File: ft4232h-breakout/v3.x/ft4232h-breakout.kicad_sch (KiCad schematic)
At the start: 32 parts, among them J3 Conn_01x03, J4 Conn_01x03, J5 JLCPCB_3.5MM_SOCKET_C18166, J6 JLCPCB_3.5MM_SOCKET_C18166, J7 JLCPCB_3.5MM_SOCKET_C18166, X1 FT4232H-MODULE

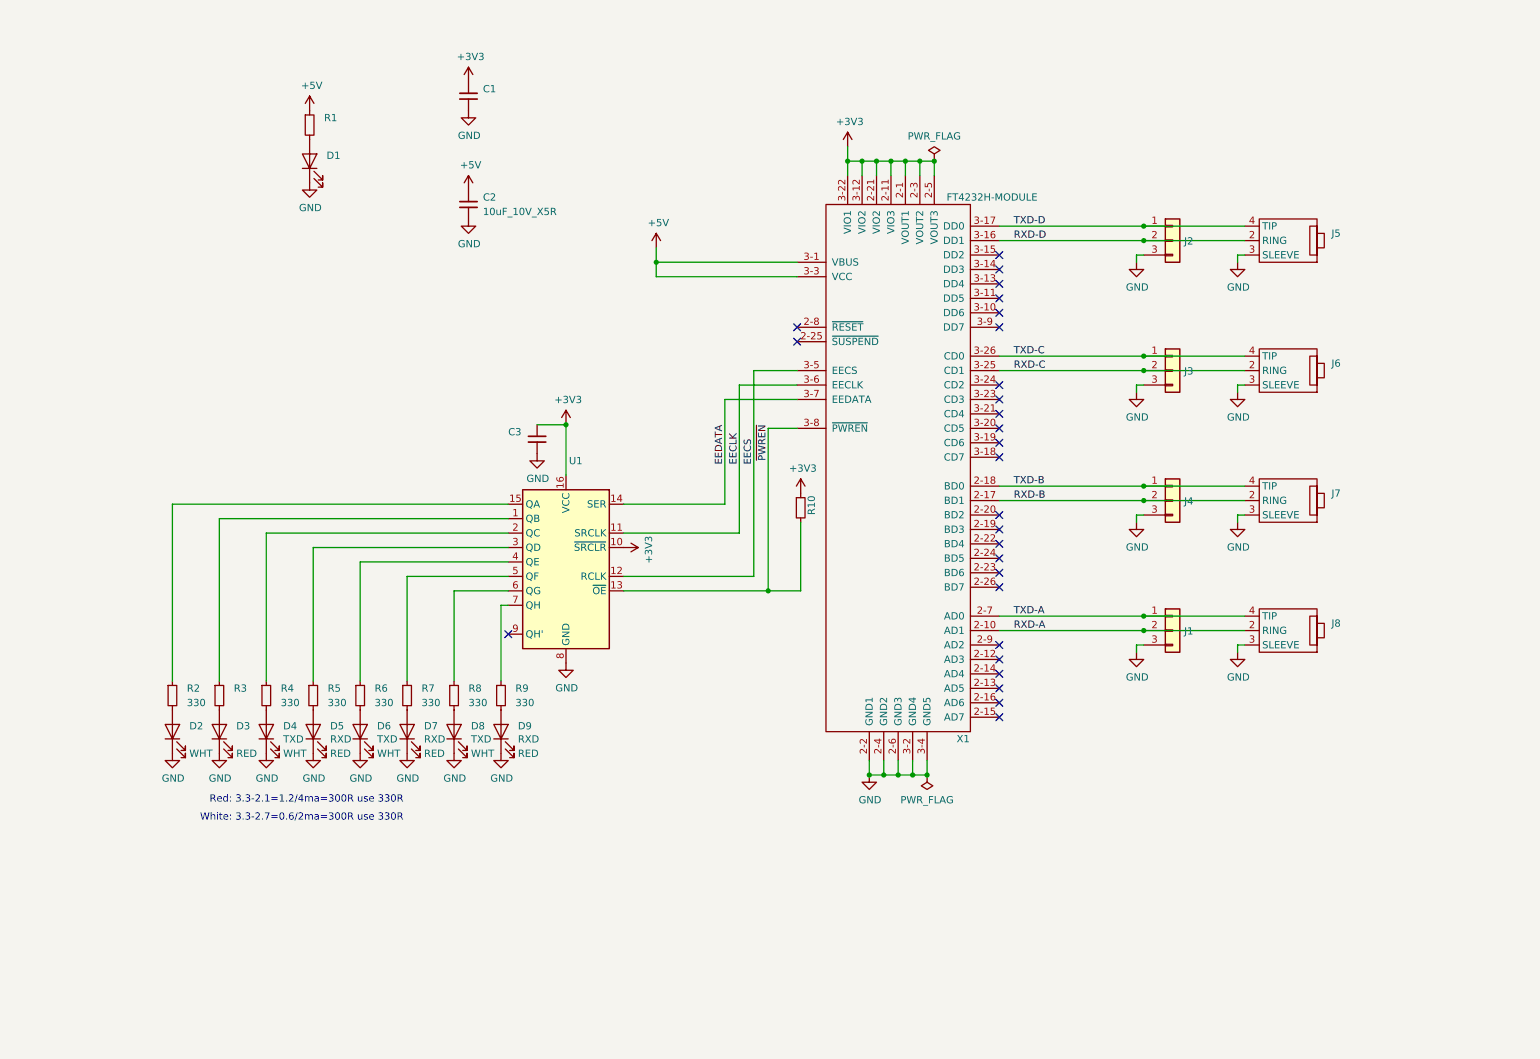
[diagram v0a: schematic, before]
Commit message: ft4232h-breakout: v3 schematic complete and reviewed
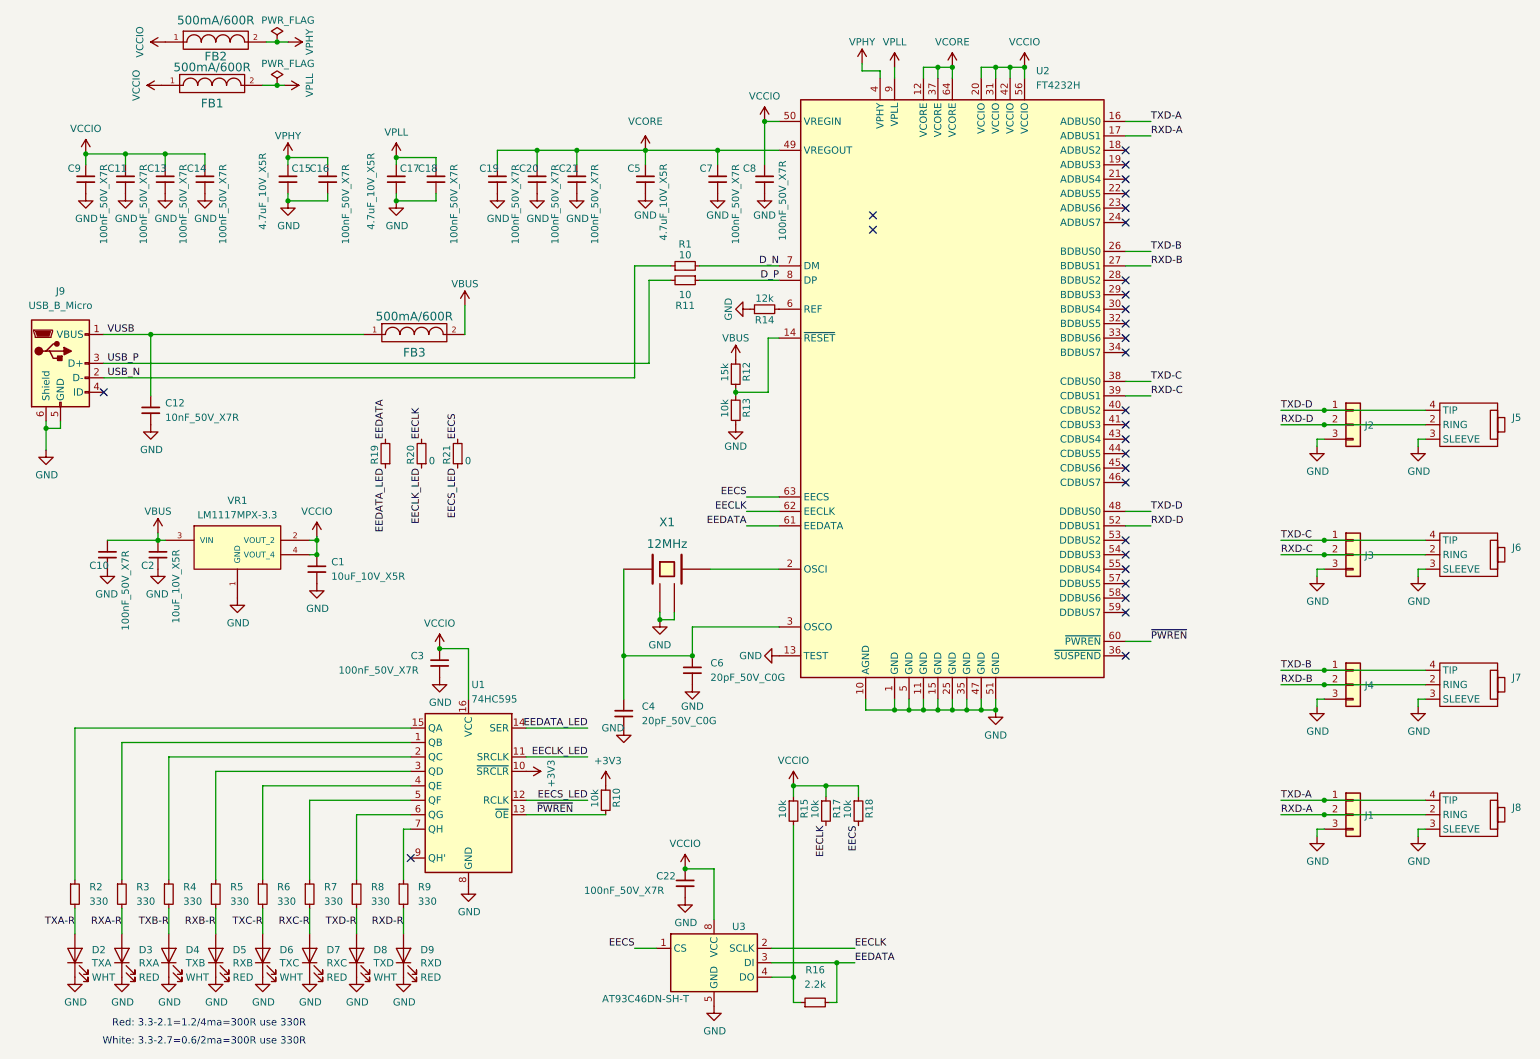
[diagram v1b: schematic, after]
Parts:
- removed D1: (no value), symbol tom-opto:LED
- removed R1: (no value), R_0402_1005Metric, symbol jlcpcb-basic-resistor-0402:1k
- removed X1: FT4232H-MODULE, tom-modules:FT4232H-MODULE, symbol tom-modules:FT4232H-MODULE
- added C10, C11, C13, C14, C16, C18, C19, C20, C21, C22, C7, C8, C9: 100nF_50V_X7R, tom-passives:C_0402_1005Metric, symbol jlcpcb-basic-capacitor-0402:100nF_50V_X7R
- added C12: 10nF_50V_X7R, tom-passives:C_0402_1005Metric, symbol jlcpcb-basic-capacitor-0402:10nF_50V_X7R
- added C15, C17, C5: 4.7uF_10V_X5R, tom-passives:C_0402_1005Metric, symbol jlcpcb-basic-capacitor-0402:4.7uF_10V_X5R
- added C4, C6: 20pF_50V_C0G, tom-passives:C_0402_1005Metric, symbol jlcpcb-basic-capacitor-0402:20pF_50V_C0G
- added FB1, FB2, FB3: 500mA/600R, tom-passives:C_0805_2012Metric, symbol tom-passives:FILTER
- added J9: USB_B_Micro, tom-connectors:USB_B_Micro_LCSC_C10418, symbol tom-connectors:USB_B_Micro
- added R1, R11: 10, tom-passives:R_0402_1005Metric, symbol jlcpcb-basic-resistor-0402:10
- added R12: 15k, tom-passives:R_0402_1005Metric, symbol jlcpcb-basic-resistor-0402:15k
- added R13, R15, R17, R18: 10k, tom-passives:R_0402_1005Metric, symbol jlcpcb-basic-resistor-0402:10k
- added R14: 12k, tom-passives:R_0402_1005Metric, symbol jlcpcb-basic-resistor-0402:12k
- added R16: 2.2k, tom-passives:R_0402_1005Metric, symbol jlcpcb-basic-resistor-0402:2.2k
- added R19: (no value), symbol jlcpcb-basic-resistor-0402:0
- added R20, R21: 0, symbol jlcpcb-basic-resistor-0402:0
- added U2: FT4232H, tom-semiconductors:TQFP-64_10x10mm_P0.5mm, symbol tom-semiconductors:FT4232H
- added U3: AT93C46DN-SH-T, tom-semiconductors:SO-8_3.9x4.9mm_P1.27mm, symbol Memory_EEPROM:93CxxA
- added VR1: LM1117MPX-3.3, tom-semiconductors:VREG_LM1117MPX-3.3, symbol tom-semiconductors:LM1117MPX-3.3
- added X1: 12MHz, tom-passives:Crystal_SMD_3225-4Pin_3.2x2.5mm, symbol tom-passives:CRYSTAL_4PIN
- C1: value (none) -> 10uF_10V_X5R; footprint C_0603_1608Metric -> tom-passives:C_0603_1608Metric
- C2: footprint C_0603_1608Metric -> tom-passives:C_0603_1608Metric
- C3: value (none) -> 100nF_50V_X7R; footprint C_0402_1005Metric -> tom-passives:C_0402_1005Metric
- D2: value (none) -> TXA; footprint (none) -> tom-opto:LED_0603_1608Metric
- D3: value (none) -> RXA; footprint (none) -> tom-opto:LED_0603_1608Metric
- D4: value TXD -> TXB
- D5: value RXD -> RXB
- D6: value TXD -> TXC
- D7: value RXD -> RXC
- J1, J2: value (none) -> Conn_01x03; footprint (none) -> tom-connectors:PinHeader_1x03_P2.54mm_Horizontal
- J8: value (none) -> JLCPCB_3.5MM_SOCKET_C18166
- R10: value (none) -> 10k; footprint R_0402_1005Metric -> tom-passives:R_0402_1005Metric
- R2, R4, R5, R6, R7, R8, R9: footprint R_0402_1005Metric -> tom-passives:R_0402_1005Metric
- R3: value (none) -> 330; footprint R_0402_1005Metric -> tom-passives:R_0402_1005Metric
- U1: value (none) -> 74HC595; footprint (none) -> tom-semiconductors:SOIC-16_4.55x10.3mm_P1.27mm
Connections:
- net +3V3: no longer C1.1, C3.2, U1.16 (VCC)
- net EECLK: now also R17.2, R20.2, U2.62 (EECLK), U3.2 (SCLK); no longer U1.11 (SRCLK)
- net EECS: now also R18.2, R21.2, U2.63 (EECS), U3.1 (CS); no longer U1.12 (RCLK)
- net EEDATA: now also R16.2, R19.2, U2.61 (EEDATA), U3.3 (DI); no longer U1.14 (SER)
- net GND: now also C10.1, C11.1, C12.2, C13.1, C14.1, C15.2, C16.1, C17.2, C18.1, C19.1, C20.1, C21.1, C22.1, C4.2, C5.2, C6.2, C7.1, C8.1, C9.1, J9.5 (GND), J9.6 (Shield), R13.2, R14.1, U2.1 (GND), U2.10 (AGND), U2.11 (GND), U2.13 (TEST), U2.15 (GND), U2.25 (GND), U2.35 (GND), U2.47 (GND), U2.5 (GND), U2.51 (GND), U3.5 (GND), VR1.1 (GND), X1.2 (GND), X1.4 (GND)
- net RXD-A: now also U2.17 (ADBUS1)
- net RXD-B: now also U2.27 (BDBUS1)
- net RXD-C: now also U2.39 (CDBUS1)
- net RXD-D: now also U2.52 (DDBUS1)
- net TXD-A: now also U2.16 (ADBUS0)
- net TXD-B: now also U2.26 (BDBUS0)
- net TXD-C: now also U2.38 (CDBUS0)
- net TXD-D: now also U2.48 (DDBUS0)
- net ~{PWREN}: now also U2.60 (~{PWREN})
- net RXD-R: now reaches D9.2 (A), R9.2
- net RXA-R: now reaches D3.2 (A), R3.2
- net TXD-R: now reaches D8.2 (A), R8.2
- net TXC-R: now reaches D6.2 (A), R6.2
- net RXB-R: now reaches D5.2 (A), R5.2
- net TXB-R: now reaches D4.2 (A), R4.2
- net TXA-R: now reaches D2.2 (A), R2.2
- net RXC-R: now reaches D7.2 (A), R7.2
- net +5V renamed VBUS
- net VBUS: now also C10.2, FB3.2, R12.1, VR1.3 (VIN)
- new net: C4.1, C6.1, U2.3 (OSCO), X1.1
- new net: U2.2 (OSCI), X1.3
- new net: R15.2, R16.1, U3.4 (DO)
- new net: R12.2, R13.1, U2.14 (~{RESET})
- new net: R14.2, U2.6 (REF)
- new net D_N: R1.2, U2.7 (DM)
- new net D_P: R11.1, U2.8 (DP)
- new net EECLK_LED: R20.1, U1.11 (SRCLK)
- new net EECS_LED: R21.1, U1.12 (RCLK)
- new net EEDATA_LED: R19.1, U1.14 (SER)
- new net USB_N: J9.2 (D-), R1.1
- new net USB_P: J9.3 (D+), R11.2
- new net VCCIO: C1.1, C11.2, C13.2, C14.2, C22.2, C3.2, C8.2, C9.2, FB1.1, FB2.1, R15.1, R17.1, R18.1, U1.16 (VCC), U2.20 (VCCIO), U2.31 (VCCIO), U2.42 (VCCIO), U2.50 (VREGIN), U2.56 (VCCIO), U3.8 (VCC), VR1.2 (VOUT_2), VR1.4 (VOUT_4)
- new net VCORE: C19.2, C20.2, C21.2, C5.1, C7.2, U2.12 (VCORE), U2.37 (VCORE), U2.49 (VREGOUT), U2.64 (VCORE)
- new net VPHY: C15.1, C16.2, FB2.2, U2.4 (VPHY)
- new net VPLL: C17.1, C18.2, FB1.2, U2.9 (VPLL)
- new net VUSB: C12.1, FB3.1, J9.1 (VBUS)
- no-connect marks 27 -> 29
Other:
- moved on the sheet: C1, C2, C3, D2, D3, D4, D5, D6, D7, D8, D9, J1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

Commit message: ft4232h-breakout: v3 at rc1
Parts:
- added D1: LED, tom-opto:LED_0603_1608Metric, symbol tom-opto:LED
- added J10: USB_C_Receptacle_USB2.0, tom-connectors:USB_C_Receptacle_LCSC_C165948, symbol tom-connectors:USB_C_Receptacle_USB2.0
- added R22: 330, tom-passives:R_0402_1005Metric, symbol jlcpcb-basic-resistor-0402:330
- added R23, R24: 5.1k, R_0402_1005Metric, symbol jlcpcb-basic-resistor-0402:5.1k
- R19: value (none) -> 0; footprint (none) -> tom-passives:R_0402_1005Metric
- R20, R21: footprint (none) -> tom-passives:R_0402_1005Metric
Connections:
- net +3V3 is gone; now on net VCCIO: R10.1, U1.10 (~{SRCLR})
- net GND: now also D1.1 (K), J10.A1 (GND), J10.A12 (GND), J10.B1 (GND), J10.B12 (GND), J10.S1 (SHIELD), R23.2, R24.2
- net USB_N: now also J10.A7 (D-), J10.B7 (D-)
- net USB_P: now also J10.A6 (D+), J10.B6 (D+)
- net VCCIO: now also R22.1
- net VUSB: now also J10.A4 (VBUS), J10.A9 (VBUS), J10.B4 (VBUS), J10.B9 (VBUS)
- net at C4.1, U2.3 (OSCO), X1.1: no longer C6.1
- net at U2.2 (OSCI), X1.3: now also C6.1
- net EED0: now reaches R15.2, R16.1, U3.4 (DO)
- net ~{RESET}: now reaches R12.2, R13.1, U2.14 (~{RESET})
- new net: J10.A5 (CC1), R24.1
- new net: J10.B5 (CC2), R23.1
- new net: D1.2 (A), R22.2
- no-connect marks 29 -> 31
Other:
- moved on the sheet: C1, C10, C2, C6, R19, R20, R21, VR1
